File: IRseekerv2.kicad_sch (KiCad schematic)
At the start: 41 parts, among them J13 Conn_01x04_Pin, J14 Conn_01x02_Pin, J15 SEL_VOLTAGE, J16 G, J17 G, J18 G, J19 G, J20 Conn_01x02_Pin, J26 Conn_01x02_Pin, J27 Conn_01x02_Pin, J28 Conn_01x02_Pin, SW1 SW_Push, SW2 SW_Push, U10 TSSP4038, U11 TSSP4038, U12 TSSP4038, U13 TSSP4038, U14 TSSP4038, U15 TSSP4038, U16 TSSP4038, U17 AMS1117-3.3, U2 CD4012, U3 STM32G431CBUx, U4 CD4012B, U5 TSSP4038, U6 TSSP4038, U7 TSSP4038, U8 TSSP4038, U9 TSSP4038, Y1 Crystal

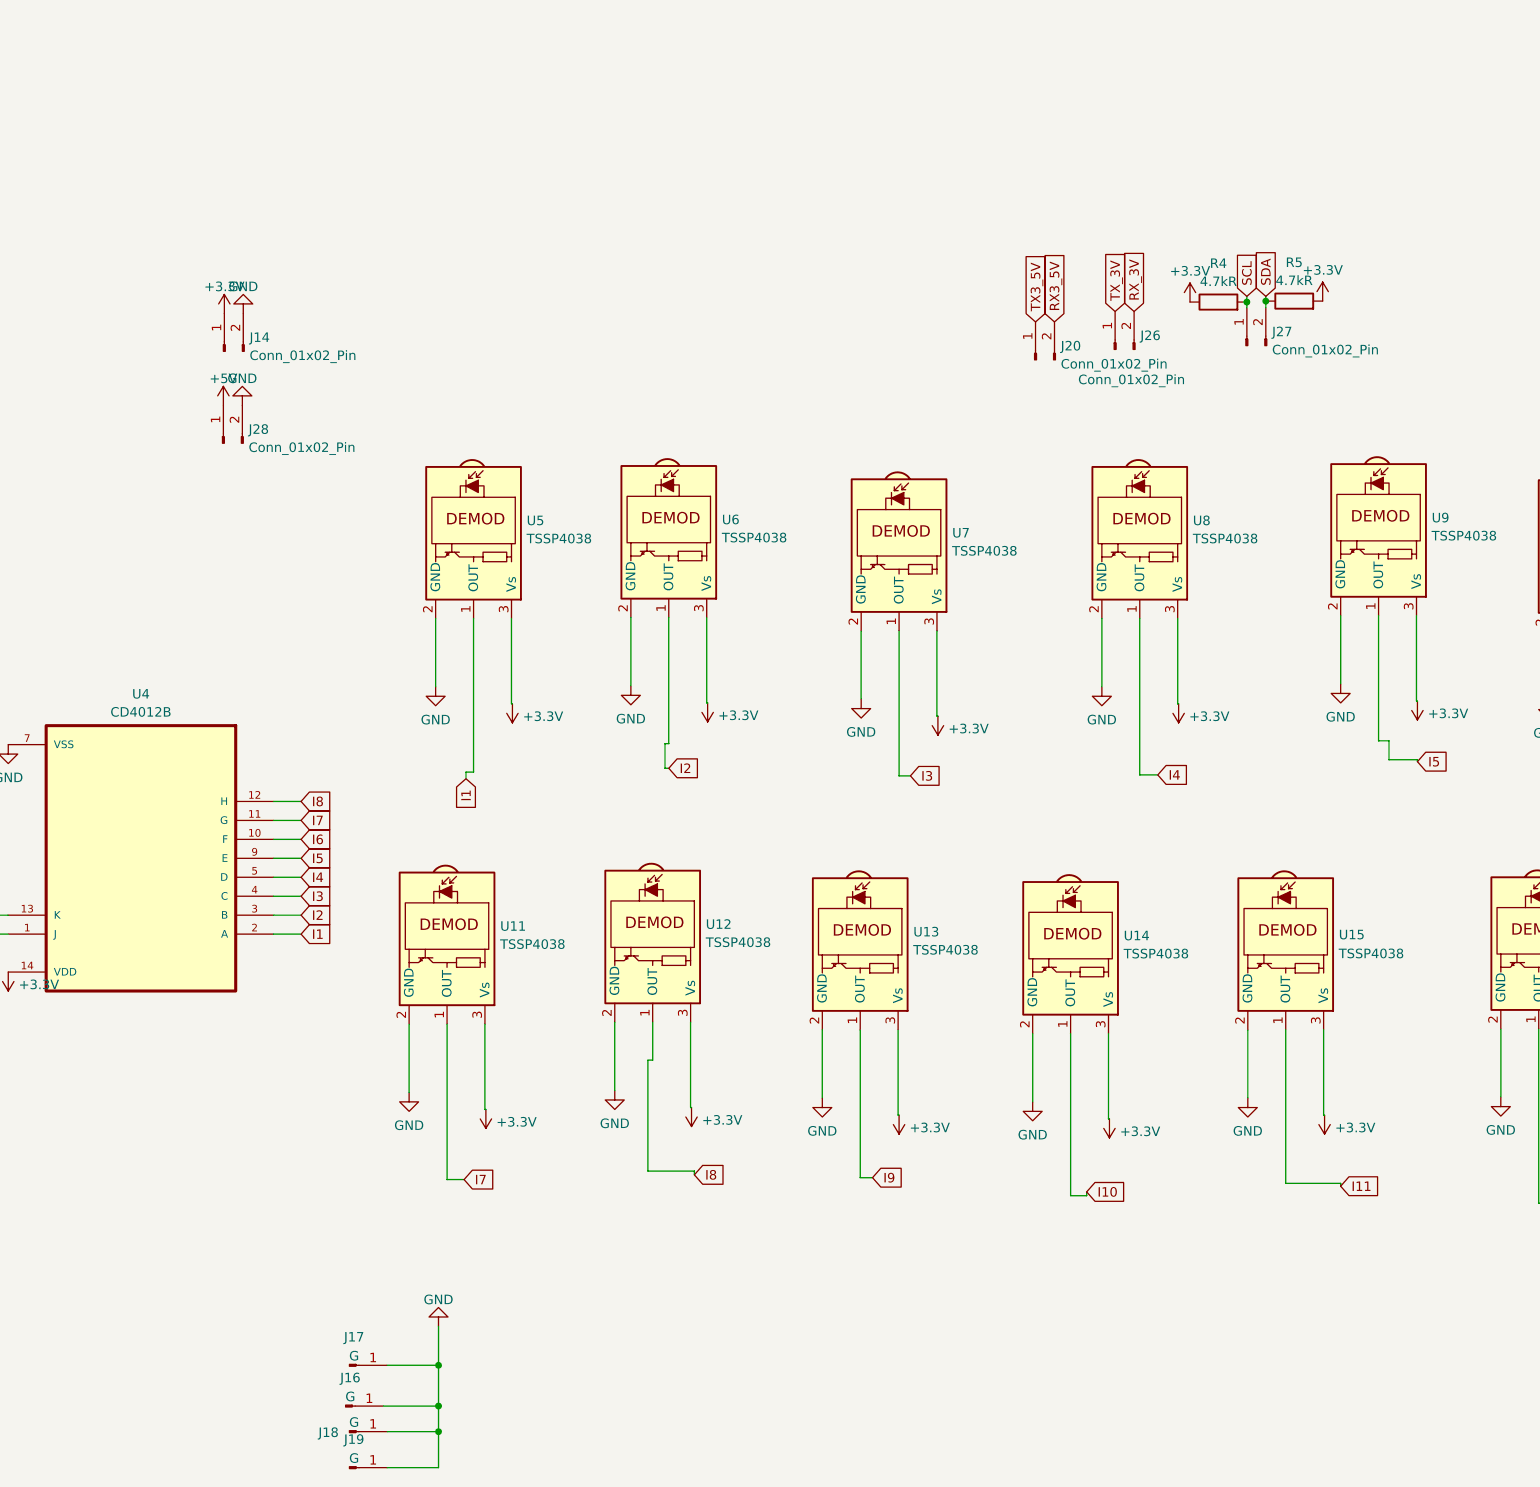
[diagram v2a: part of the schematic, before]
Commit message: Disconnected mounting holes from ground, reroute some connections because of I2C pullups
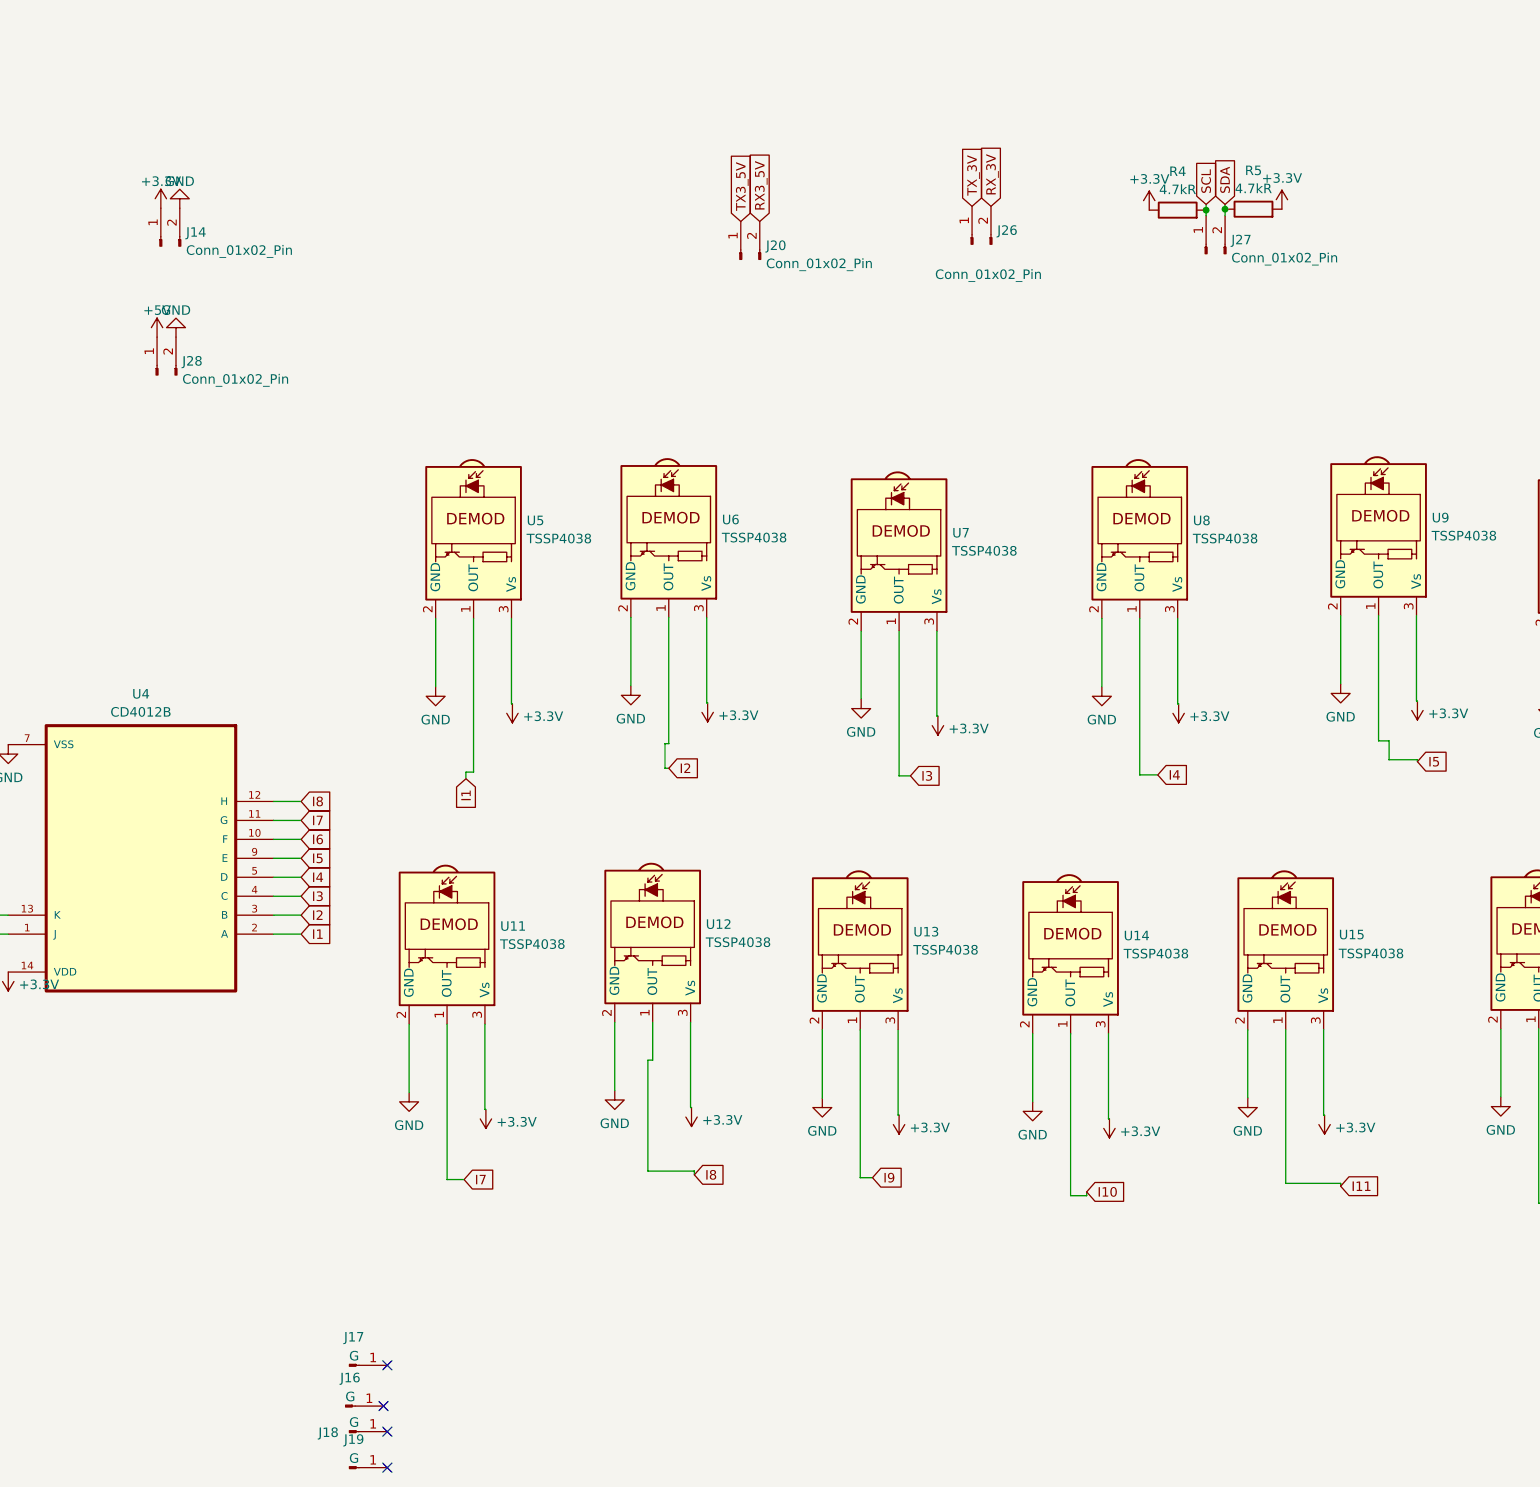
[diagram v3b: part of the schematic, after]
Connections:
- net GND: no longer J16.1 (Pin_1), J17.1 (Pin_1), J18.1 (Pin_1), J19.1 (Pin_1)
- no-connect marks 0 -> 4
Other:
- moved on the sheet: J14, J20, J26, J27, J28, R4, R5

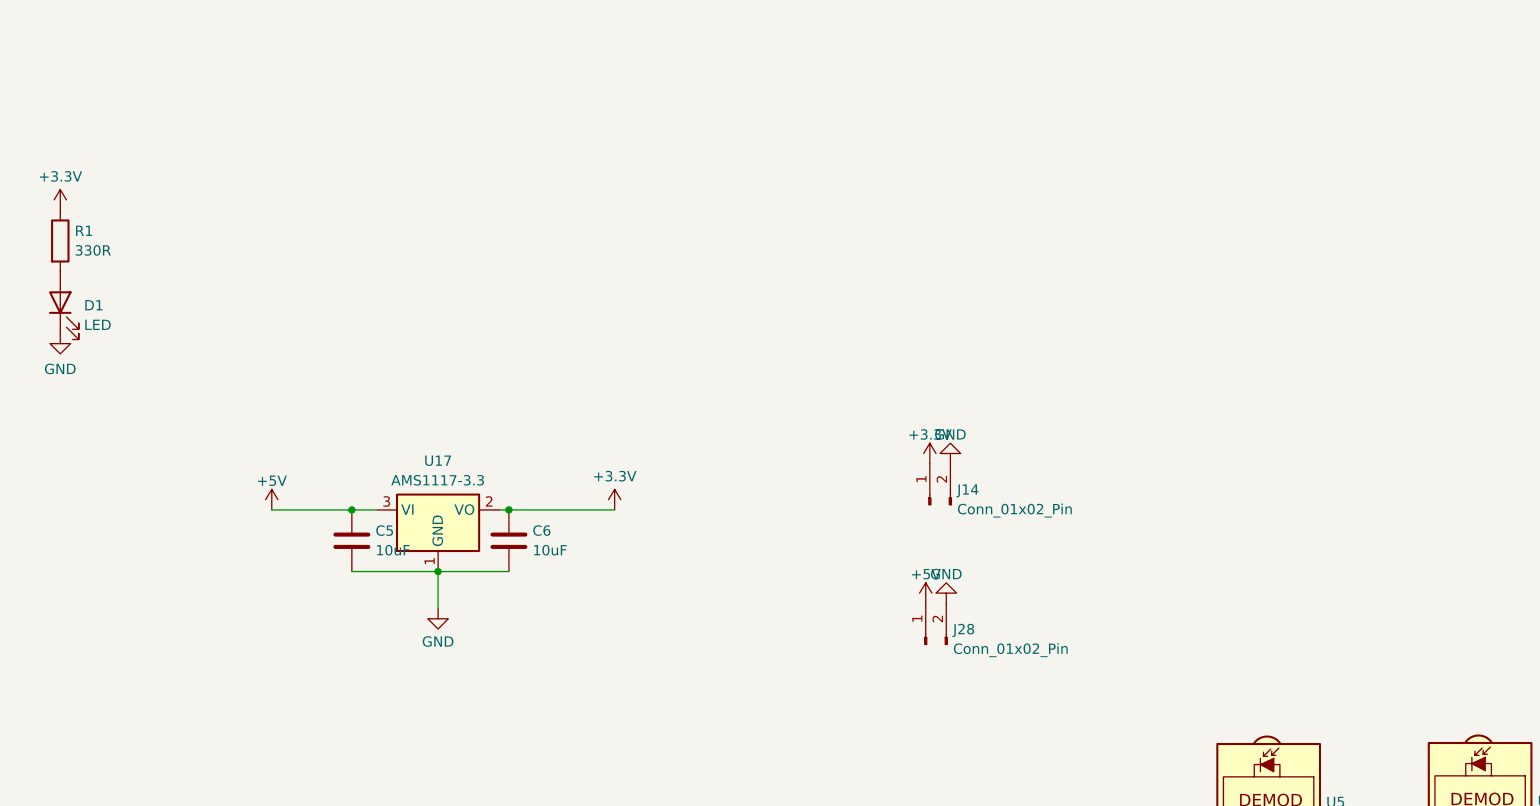
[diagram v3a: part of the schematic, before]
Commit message: Add forgotten decoupling capacitors and change footprints
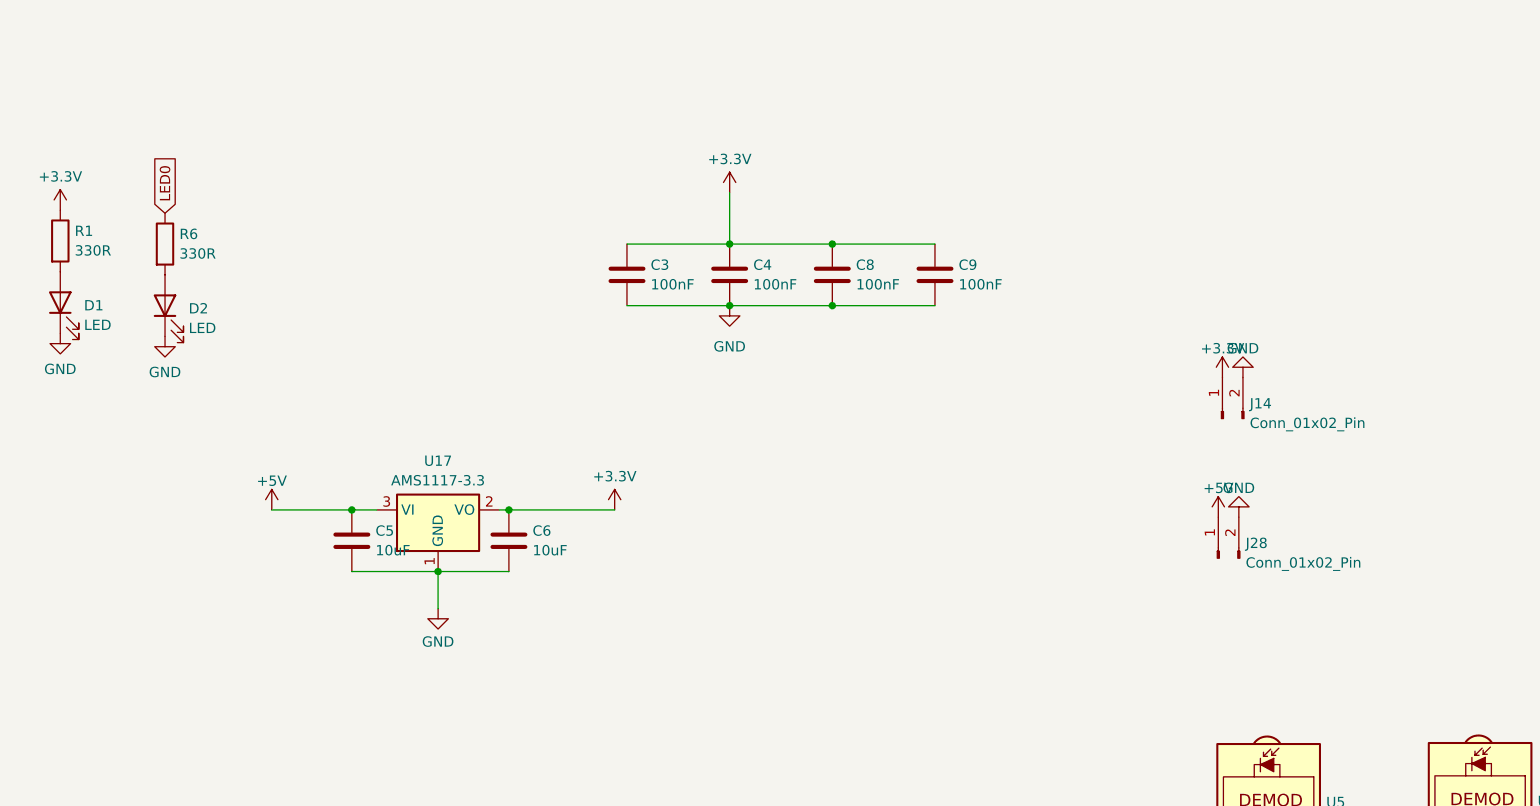
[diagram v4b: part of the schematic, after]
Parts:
- added C3, C4, C8, C9: 100nF, Capacitor_SMD:C_0603_1608Metric, symbol Device:C
- added D2: LED, LED_THT:LED_D5.0mm, symbol Device:LED
- added R6: 330R, Resistor_SMD:R_0603_1608Metric, symbol Device:R
- C1, C2, C5, C6: footprint Capacitor_THT:C_Disc_D3.0mm_W1.6mm_P2.50mm -> Capacitor_SMD:C_0603_1608Metric
- D1: footprint LED_THT:LED_D3.0mm -> LED_THT:LED_D5.0mm
- R1, R2, R3: footprint Resistor_THT:R_Axial_DIN0204_L3.6mm_D1.6mm_P1.90mm_Vertical -> Resistor_SMD:R_0603_1608Metric
- R4, R5: footprint Resistor_THT:R_Axial_DIN0204_L3.6mm_D1.6mm_P2.54mm_Vertical -> Resistor_SMD:R_0603_1608Metric
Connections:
- net +3.3V: now also C3.2, C4.2, C8.2, C9.2
- net GND: now also C3.1, C4.1, C8.1, C9.1, D2.1 (K)
- net LED0: now also R6.1
- new net: D2.2 (A), R6.2
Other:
- moved on the sheet: J14, J28

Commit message: Reworked to some smd components
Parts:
- added C10: 4.7uF, Capacitor_SMD:C_0603_1608Metric, symbol Device:C
- added C11: 100nF, Capacitor_SMD:C_0603_1608Metric, symbol Device:C
- C7: footprint Capacitor_THT:C_Disc_D3.0mm_W1.6mm_P2.50mm -> Capacitor_SMD:C_0603_1608Metric
- D1, D2: footprint LED_THT:LED_D5.0mm -> LED_SMD:LED_0603_1608Metric
- U2: value CD4012 -> HEF4082BT; footprint CD70xx:DIP794W45P254L1969H508Q14 -> Package_SO:SO-14_3.9x8.65mm_P1.27mm
- U4: value CD4012B -> HEF4082BT; footprint CD70xx:DIP794W45P254L1969H508Q14 -> Package_SO:SO-14_3.9x8.65mm_P1.27mm
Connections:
- net +3.3V: now also C10.2, C11.2
- net GND: now also C10.1, C11.1
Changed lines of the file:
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@@
   (junction (at 72.263 137.922) (diameter 0) (color 0 0 0 0)
   )
+  (junction (at 190.5 74.93) (diameter 0) (color 0 0 0 0)
+  )
   (junction (at 118.364 100.203) (diameter 0) (color 0 0 0 0)
   )
@@
   (junction (at 59.182 45.974) (diameter 0) (color 0 0 0 0)
   )
+  (junction (at 190.5 67.31) (diameter 0) (color 0 0 0 0)
+  )
   (junction (at 165.1 74.93) (diameter 0) (color 0 0 0 0)
   )
   (junction (at 332.486 94.615) (diameter 0) (color 0 0 0 0)
   )
+  (junction (at 152.4 74.93) (diameter 0) (color 0 0 0 0)
+  )
+  (junction (at 152.4 67.31) (diameter 0) (color 0 0 0 0)
+  )
   (no_connect (at 220.218 249.555))
   (no_connect (at 220.218 258.445))
@@
     (stroke (width 0) (type default))
   )
+  (wire (pts (xy 190.5 74.93) (xy 203.2 74.93))
+    (stroke (width 0) (type default))
+  )
   (wire (pts (xy 358.267 168.402) (xy 358.267 168.656))
     (stroke (width 0) (type default))
@@
     (stroke (width 0) (type default))
   )
+  (wire (pts (xy 140.97 67.31) (xy 152.4 67.31))
+    (stroke (width 0) (type default))
+  )
   (wire (pts (xy 358.14 160.528) (xy 358.267 160.528))
     (stroke (width 0) (type default))
@@
     (stroke (width 0) (type default))
   )
+  (wire (pts (xy 140.97 74.93) (xy 152.4 74.93))
+    (stroke (width 0) (type default))
+  )
   (wire (pts (xy 38.1 33.909) (xy 38.1 34.925))
     (stroke (width 0) (type default))
@@
     (stroke (width 0) (type default))
   )
+  (wire (pts (xy 190.5 67.31) (xy 203.2 67.31))
+    (stroke (width 0) (type default))
+  )
   (wire (pts (xy 236.855 149.479) (xy 236.855 160.909))
     (stroke (width 0) (type default))
@@
     )
   )
+  (symbol (lib_id "Device:C") (at 203.2 71.12 180) (unit 1)
+    (in_bom yes) (on_board yes) (dnp no) (fields_autoplaced)
+    (property "Reference" "C10" (at 206.121 69.9079 0)
+      (effects (font (size 1.27 1.27)) (justify right))
+    )
+    (property "Value" "4.7uF" (at 206.121 72.3321 0)
+      (effects (font (size 1.27 1.27)) (justify right))
+    )
+    (property "Footprint" "Capacitor_SMD:C_0603_1608Metric" (at 202.2348 67.31 0)
+      (effects (font (size 1.27 1.27)) hide)
+    )
+    (property "Datasheet" "~" (at 203.2 71.12 0)
+      (effects (font (size 1.27 1.27)) hide)
+    )
+    (pin "1")
+    (pin "2")
+    (instances
+      (project "IRseekerv2"
+        (path "/c83ed66b-8f4f-4f32-bd83-eab9fc6ed48e"
+          (reference "C10") (unit 1)
+        )
+      )
+    )
+  )
   (symbol (lib_id "Device:Crystal") (at 34.544 161.798 270) (unit 1)
     (in_bom yes) (on_board yes) (dnp no)
@@
   (symbol (lib_id "CD4012:CD4012BE") (at 187.198 181.61 180) (unit 1)
     (in_bom yes) (on_board yes) (dnp no) (fields_autoplaced)
-    (property "Reference" "U4" (at 187.198 159.6077 0)
+    (property "Reference" "U4" (at 187.198 158.75 0)
       (effects (font (size 1.27 1.27)))
     )
-    (property "Value" "CD4012B" (at 187.198 162.0319 0)
+    (property "Value" "HEF4082BT" (at 187.198 161.29 0)
       (effects (font (size 1.27 1.27)))
     )
-    (property "Footprint" "CD70xx:DIP794W45P254L1969H508Q14" (at 187.198 181.61 0)
+    (property "Footprint" "Package_SO:SO-14_3.9x8.65mm_P1.27mm" (at 187.198 181.61 0)
       (effects (font (size 1.27 1.27)) (justify bottom) hide)
     )
@@
       (effects (font (size 1.27 1.27)) (justify right))
     )
-    (property "Footprint" "LED_THT:LED_D5.0mm" (at 95.25 74.93 0)
+    (property "Footprint" "LED_SMD:LED_0603_1608Metric" (at 95.25 74.93 0)
       (effects (font (size 1.27 1.27)) hide)
     )
@@
   (symbol (lib_id "CD4012:CD4012BE") (at 120.904 199.644 180) (unit 1)
     (in_bom yes) (on_board yes) (dnp no) (fields_autoplaced)
-    (property "Reference" "U2" (at 120.904 177.6417 0)
+    (property "Reference" "U2" (at 120.904 176.53 0)
       (effects (font (size 1.27 1.27)))
     )
-    (property "Value" "CD4012" (at 120.904 180.0659 0)
+    (property "Value" "HEF4082BT" (at 120.904 179.07 0)
       (effects (font (size 1.27 1.27)))
     )
-    (property "Footprint" "CD70xx:DIP794W45P254L1969H508Q14" (at 120.904 199.644 0)
+    (property "Footprint" "Package_SO:SO-14_3.9x8.65mm_P1.27mm" (at 120.904 199.644 0)
       (effects (font (size 1.27 1.27)) (justify bottom) hide)
     )
@@
       (effects (font (size 1.27 1.27)) (justify right))
     )
-    (property "Footprint" "LED_THT:LED_D5.0mm" (at 82.296 74.549 0)
+    (property "Footprint" "LED_SMD:LED_0603_1608Metric" (at 82.296 74.549 0)
       (effects (font (size 1.27 1.27)) hide)
     )
@@
       (effects (font (size 1.27 1.27)))
     )
-    (property "Footprint" "Capacitor_THT:C_Disc_D3.0mm_W1.6mm_P2.50mm" (at 45.085 55.9562 0)
+    (property "Footprint" "Capacitor_SMD:C_0603_1608Metric" (at 45.085 55.9562 0)
       (effects (font (size 1.27 1.27)) hide)
     )
@@
         )
       )
+    )
+  )
+  (symbol (lib_id "Device:C") (at 140.97 71.12 180) (unit 1)
+    (in_bom yes) (on_board yes) (dnp no) (fields_autoplaced)
+    (property "Reference" "C11" (at 143.891 69.9079 0)
+      (effects (font (size 1.27 1.27)) (justify right))
+    )
+    (property "Value" "100nF" (at 143.891 72.3321 0)
+      (effects (font (size 1.27 1.27)) (justify right))
+    )
+    (property "Footprint" "Capacitor_SMD:C_0603_1608Metric" (at 140.0048 67.31 0)
+      (effects (font (size 1.27 1.27)) hide)
+    )
+    (property "Datasheet" "~" (at 140.97 71.12 0)
+      (effects (font (size 1.27 1.27)) hide)
+    )
+    (pin "1")
+    (pin "2")
+    (instances
+      (project "IRseekerv2"
+        (path "/c83ed66b-8f4f-4f32-bd83-eab9fc6ed48e"
+          (reference "C11") (unit 1)
+        )
+      )
